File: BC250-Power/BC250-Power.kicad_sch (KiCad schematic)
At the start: 41 parts, among them J1 Conn_01x02_Pin, J2 Conn_01x02_Pin, J3 Conn_01x02_Pin, J4 Conn_01x03_Pin, J5 Conn_02x04_Odd_Even, J6 Conn_02x25_Row_Letter_First, J7 Conn_01x02_Pin, J8 Conn_01x02_Pin, M1 Fan_4pin, M2 Fan_4pin, M3 Fan_4pin, M4 Fan_4pin, Q1 BSS138, SW1 SW_Push, U1 NE555D, U2 TL082, U3 74LVC2G14, U4 L78L05_SO8

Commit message: Add values for fan circuit passives
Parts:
- added Q2: BSS138, Package_TO_SOT_SMD:SOT-23, symbol Transistor_FET:BSS138
- added R14: 10k, Resistor_SMD:R_0603_1608Metric, symbol Device:R
- C1, C2: value C -> 1uF
- R1, R2: value R -> 220
- R10, R13: value 10K -> 10k
- R11: value 1K -> 1k
- R12: value 100K -> 100k
- R3: value 100k -> 56k
- R6: value R -> 150
- R7: value R -> 2k
- R8, R9: value R -> 1k
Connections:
- net +5V: now also R14.1
- net GND: now also Q2.2 (S)
- net PWM_OUT: now also Q2.3 (D), R14.2; no longer R9.1, U2.7
- net at R3.2, R4.2, R5.1: now also U2.6 (-); no longer U2.5 (+)
- net at C3.1, R7.2, U1.2 (TR)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: now also U2.5 (+); no longer U2.6 (-)
- new net: Q2.1 (G), R9.1, U2.7
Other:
- note added: "Added the driver MOSFET to be sure to get down to the negative rail (cheap op-amps don't make it down under 0.7V or so). With assembly costs, it may make sense to use a rail-to-rail op-amp like the MCP6497. Note that the MOSFET is an inverter."
- note added: "Circuit from https://electronics.stackexchange.com/questions/186841"
- note added: "R/C values chosen from experimentation in Falstad simulator; could be improved (https://tinyurl.com/28phlmzg)"
- note added: "R7 = 0.481/(F*C) = 1923 (at 2000, F becomes 24kHz) R8 = R7 / 2 = 1000 R6 = 0.15 * R8 = 150"
- moved on the sheet: U2B

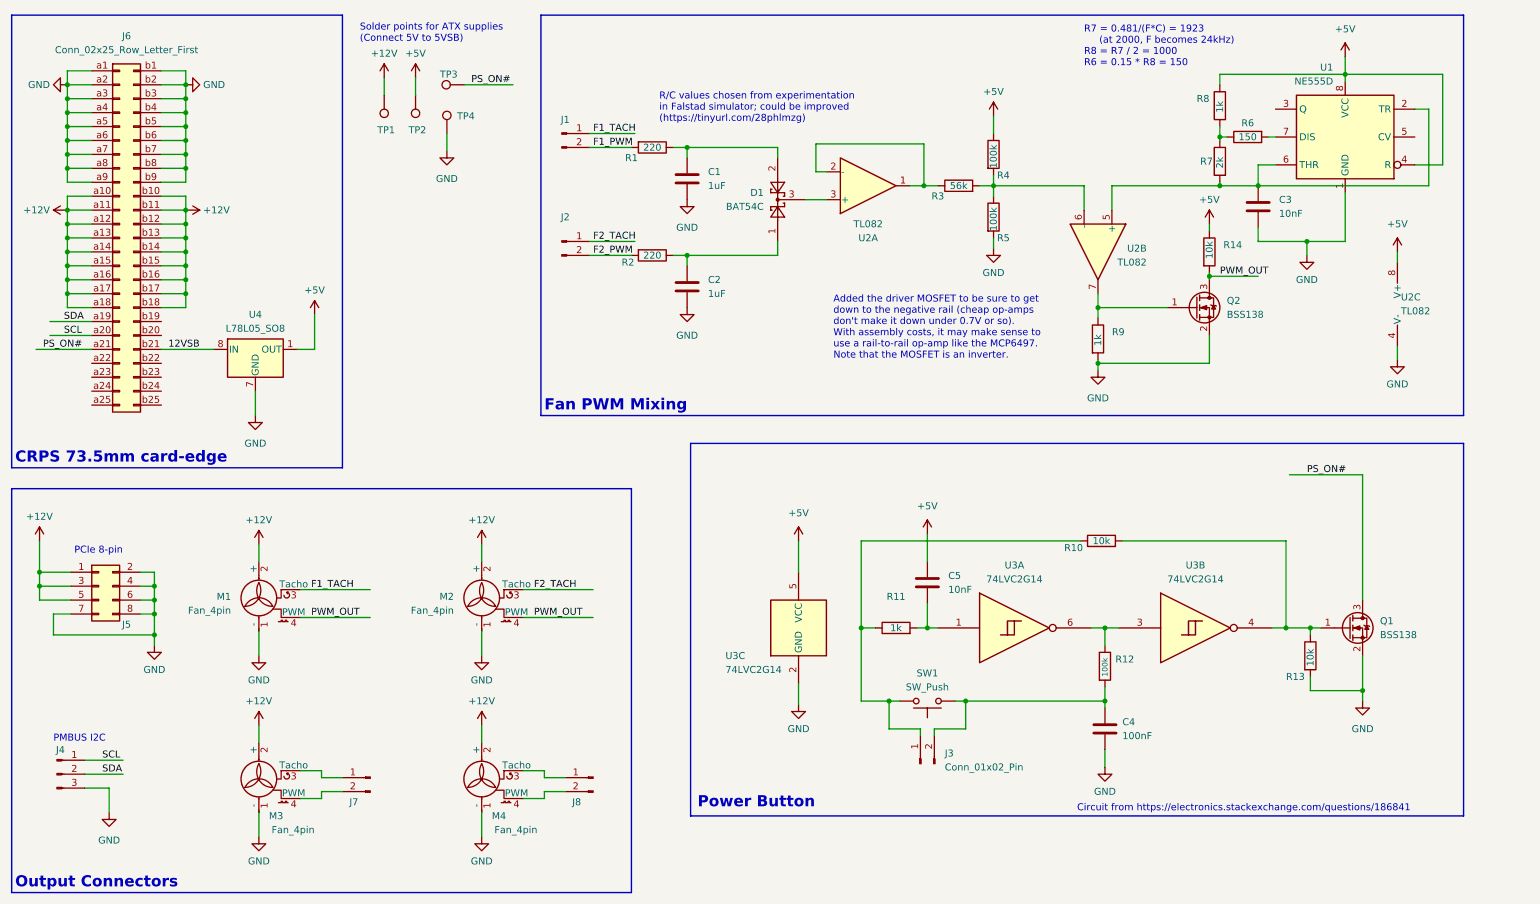
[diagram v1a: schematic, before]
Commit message: Add and associate S-50L-2.54-5 model
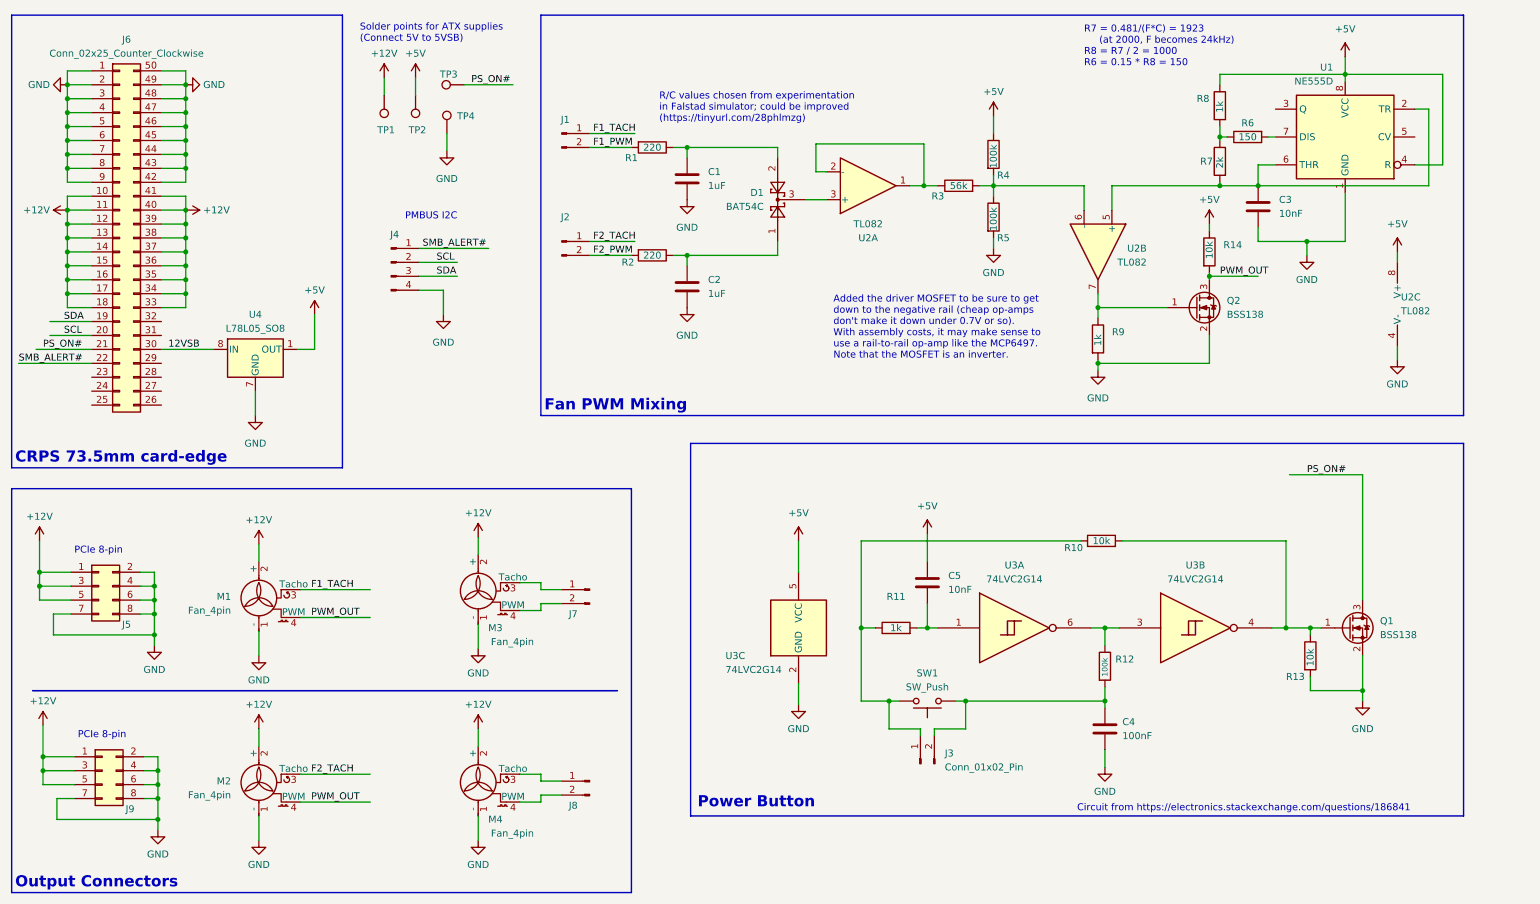
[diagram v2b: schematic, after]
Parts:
- removed J4: Conn_01x03_Pin, Connector_PinHeader_2.54mm:PinHeader_1x03_P2.54mm_Vertical, symbol Connector:Conn_01x03_Pin
- removed J6: Conn_02x25_Row_Letter_First, symbol Connector_Generic:Conn_02x25_Row_Letter_First
- added J4: Conn_01x04_Pin, Connector_PinHeader_2.54mm:PinHeader_1x04_P2.54mm_Vertical, symbol Connector:Conn_01x04_Pin
- added J6: Conn_02x25_Counter_Clockwise, BC250-Footprints:S-50L-2.54-5, symbol Connector_Generic:Conn_02x25_Counter_Clockwise
- added J9: Conn_02x04_Odd_Even, symbol Connector_Generic:Conn_02x04_Odd_Even
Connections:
- net +12V: now also J6.10 (Pin_10), J6.11 (Pin_11), J6.12 (Pin_12), J6.13 (Pin_13), J6.14 (Pin_14), J6.15 (Pin_15), J6.16 (Pin_16), J6.17 (Pin_17), J6.18 (Pin_18), J6.33 (Pin_33), J6.34 (Pin_34), J6.35 (Pin_35), J6.36 (Pin_36), J6.37 (Pin_37), J6.38 (Pin_38), J6.39 (Pin_39), J6.40 (Pin_40), J6.41 (Pin_41), J9.1 (Pin_1), J9.3 (Pin_3), J9.5 (Pin_5)
- net 12VSB: now also J6.30 (Pin_30)
- net GND: now also J4.4 (Pin_4), J6.1 (Pin_1), J6.2 (Pin_2), J6.3 (Pin_3), J6.4 (Pin_4), J6.42 (Pin_42), J6.43 (Pin_43), J6.44 (Pin_44), J6.45 (Pin_45), J6.46 (Pin_46), J6.47 (Pin_47), J6.48 (Pin_48), J6.49 (Pin_49), J6.5 (Pin_5), J6.50 (Pin_50), J6.6 (Pin_6), J6.7 (Pin_7), J6.8 (Pin_8), J6.9 (Pin_9), J9.2 (Pin_2), J9.4 (Pin_4), J9.6 (Pin_6), J9.7 (Pin_7), J9.8 (Pin_8)
- net PS_ON#: now also J6.21 (Pin_21)
- net SCL: now also J4.2 (Pin_2), J6.20 (Pin_20)
- net SDA: now also J4.3 (Pin_3), J6.19 (Pin_19)
- new net SMB_ALERT#: J4.1 (Pin_1), J6.22 (Pin_22)
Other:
- moved on the sheet: J7, J8, M2, M3, M4

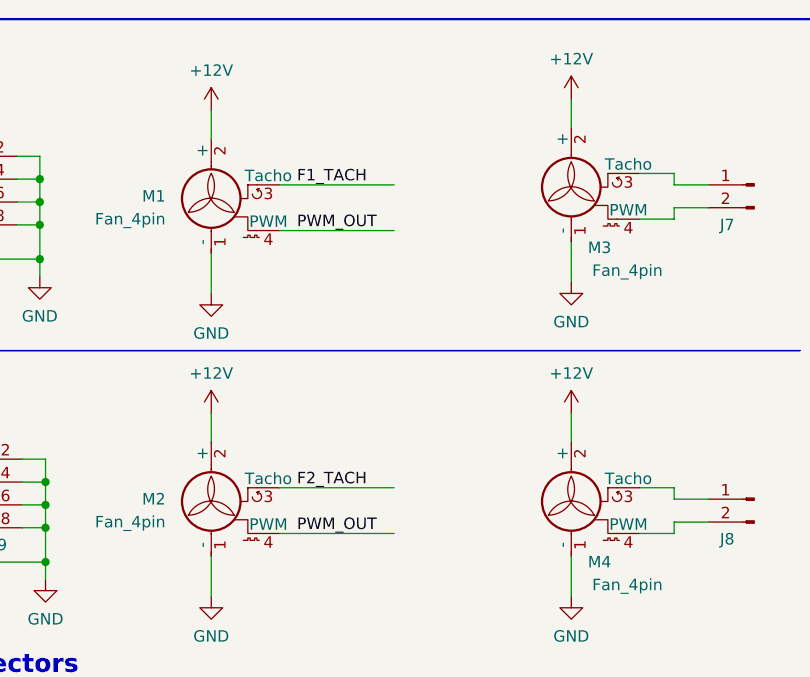
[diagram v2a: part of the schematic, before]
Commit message: Update to KiCad 9 and redo holes in card-edge footprint
Kicad 7 doesn't render shells in STEPs correctly
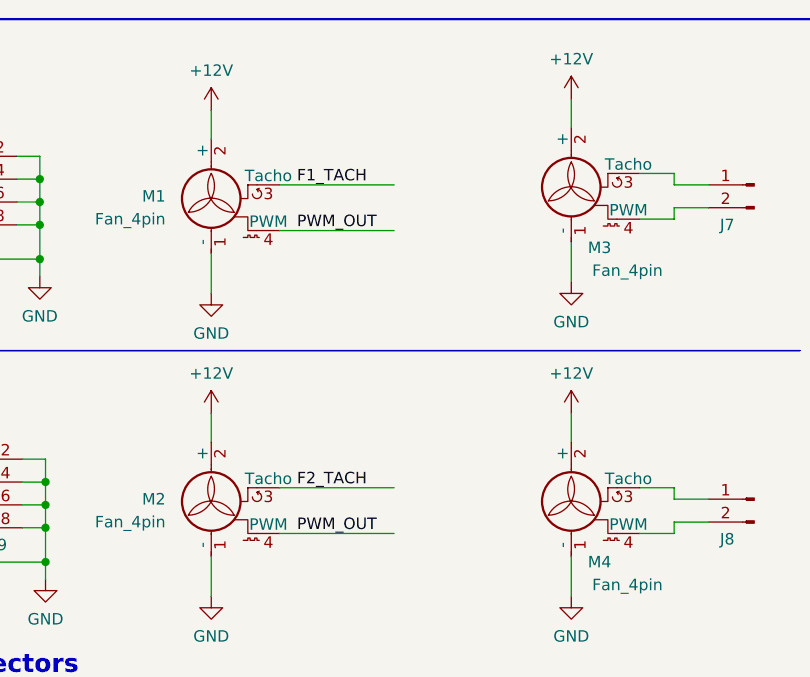
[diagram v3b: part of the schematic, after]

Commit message: Start layout and fix pinning
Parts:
- removed Q1: BSS138, Package_TO_SOT_SMD:SOT-23, symbol Transistor_FET:BSS138
- removed R13: 10k, Resistor_SMD:R_0603_1608Metric, symbol Device:R
- J5, J9: footprint (none) -> BC250-Footprints:GPU-8P-PCB; symbol Connector_Generic:Conn_02x04_Odd_Even -> Connector_Generic:Conn_02x04_Top_Bottom
- SW1: footprint (none) -> Button_Switch_SMD:SW_SPST_TL3305A
- TP1, TP2, TP3, TP4: footprint (none) -> TestPoint:TestPoint_Loop_D2.60mm_Drill1.6mm_Beaded
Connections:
- net +12V: now also J5.2 (Pin_2), J6.42 (Pin_42), J6.43 (Pin_43), J6.8 (Pin_8), J6.9 (Pin_9), J9.2 (Pin_2); no longer J5.5 (Pin_5), J6.17 (Pin_17), J6.18 (Pin_18), J6.33 (Pin_33), J6.34 (Pin_34), J9.5 (Pin_5)
- net 12VSB: now also J6.46 (Pin_46); no longer J6.30 (Pin_30)
- net GND: now also J5.5 (Pin_5), J6.17 (Pin_17), J6.18 (Pin_18), J6.19 (Pin_19), J6.20 (Pin_20), J6.21 (Pin_21), J6.22 (Pin_22), J6.23 (Pin_23), J6.24 (Pin_24), J6.25 (Pin_25), J6.26 (Pin_26), J6.27 (Pin_27), J6.28 (Pin_28), J6.29 (Pin_29), J6.30 (Pin_30), J6.31 (Pin_31), J6.32 (Pin_32), J6.33 (Pin_33), J6.34 (Pin_34), J9.5 (Pin_5); no longer J5.2 (Pin_2), J6.1 (Pin_1), J6.2 (Pin_2), J6.3 (Pin_3), J6.4 (Pin_4), J6.42 (Pin_42), J6.43 (Pin_43), J6.44 (Pin_44), J6.45 (Pin_45), J6.46 (Pin_46), J6.47 (Pin_47), J6.48 (Pin_48), J6.49 (Pin_49), J6.5 (Pin_5), J6.50 (Pin_50), J6.6 (Pin_6), J6.7 (Pin_7), J6.8 (Pin_8), J6.9 (Pin_9), J9.2 (Pin_2)
- net PS_ON#: now also J6.5 (Pin_5), R10.2, U3.4; no longer J6.21 (Pin_21)
- net SCL: now also J6.6 (Pin_6); no longer J6.20 (Pin_20)
- net SDA: now also J6.7 (Pin_7); no longer J6.19 (Pin_19)
- net SMB_ALERT#: now also J6.4 (Pin_4); no longer J6.22 (Pin_22)
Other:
- moved on the sheet: C1, C2, C3, C4, C5, D1, J1, J2, J3, J4, J5, J6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

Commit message: First pass at routing
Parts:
- removed J7, J8: Conn_01x02_Pin, Connector_PinHeader_2.54mm:PinHeader_1x02_P2.54mm_Horizontal, symbol Connector:Conn_01x02_Pin
- removed M3, M4: Fan_4pin, Connector:FanPinHeader_1x04_P2.54mm_Vertical, symbol Motor:Fan_4pin
- J4: footprint Connector_PinHeader_2.54mm:PinHeader_1x04_P2.54mm_Vertical -> Connector_PinHeader_2.54mm:PinHeader_1x04_P2.54mm_Horizontal
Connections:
- net F1_PWM: now also J1.1 (Pin_1); no longer J1.2 (Pin_2)
- net F1_TACH: now also J1.2 (Pin_2); no longer J1.1 (Pin_1)
- net GND: now also J4.1 (Pin_1); no longer J4.4 (Pin_4)
- net SCL: now also J4.3 (Pin_3); no longer J4.2 (Pin_2)
- net SDA: now also J4.2 (Pin_2); no longer J4.3 (Pin_3)
- net SMB_ALERT#: now also J4.4 (Pin_4); no longer J4.1 (Pin_1)
- net at C2.1, R2.1: now also D1.2; no longer D1.1
- net at C1.1, R1.1: now also D1.1; no longer D1.2
- net at C4.1, R12.2: now also J3.1 (Pin_1), SW1.2; no longer J3.2 (Pin_2), SW1.1
- net at R10.1, R11.1: now also J3.2 (Pin_2), SW1.1; no longer J3.1 (Pin_1), SW1.2
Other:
- moved on the sheet: C4, C5, J3, J4, R10, R11, R12, SW1, TP1, TP2, TP3, TP4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

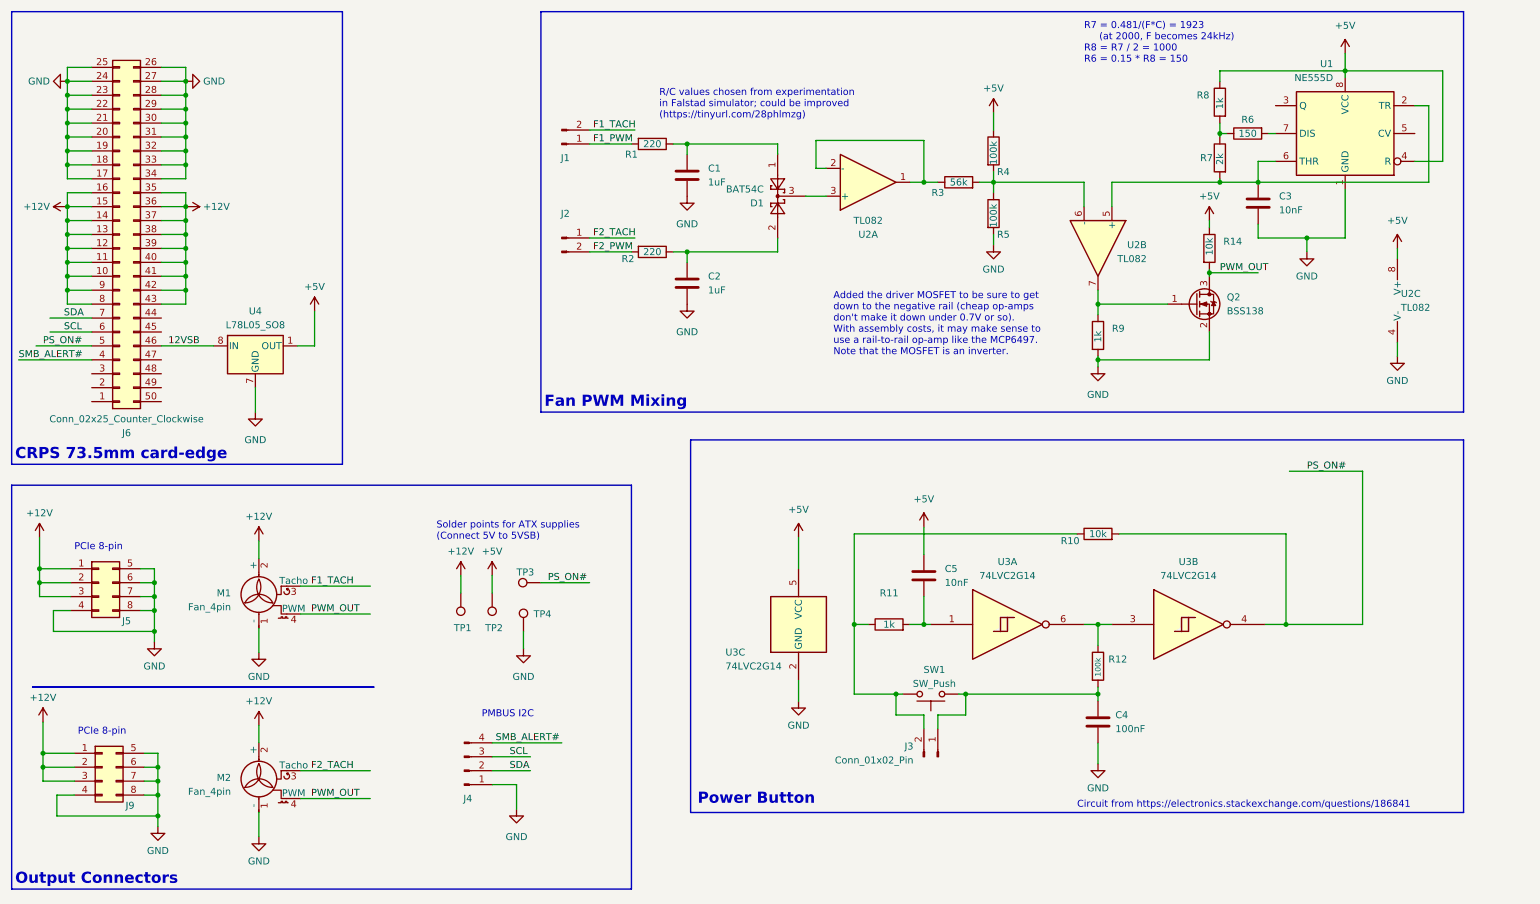
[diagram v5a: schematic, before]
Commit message: Add V0.2 of dual BC-250 CRPS breakout
- Organize fab layer
- Un-mirror edge connector (was reversing 12VSB and PS_ON# - oops)
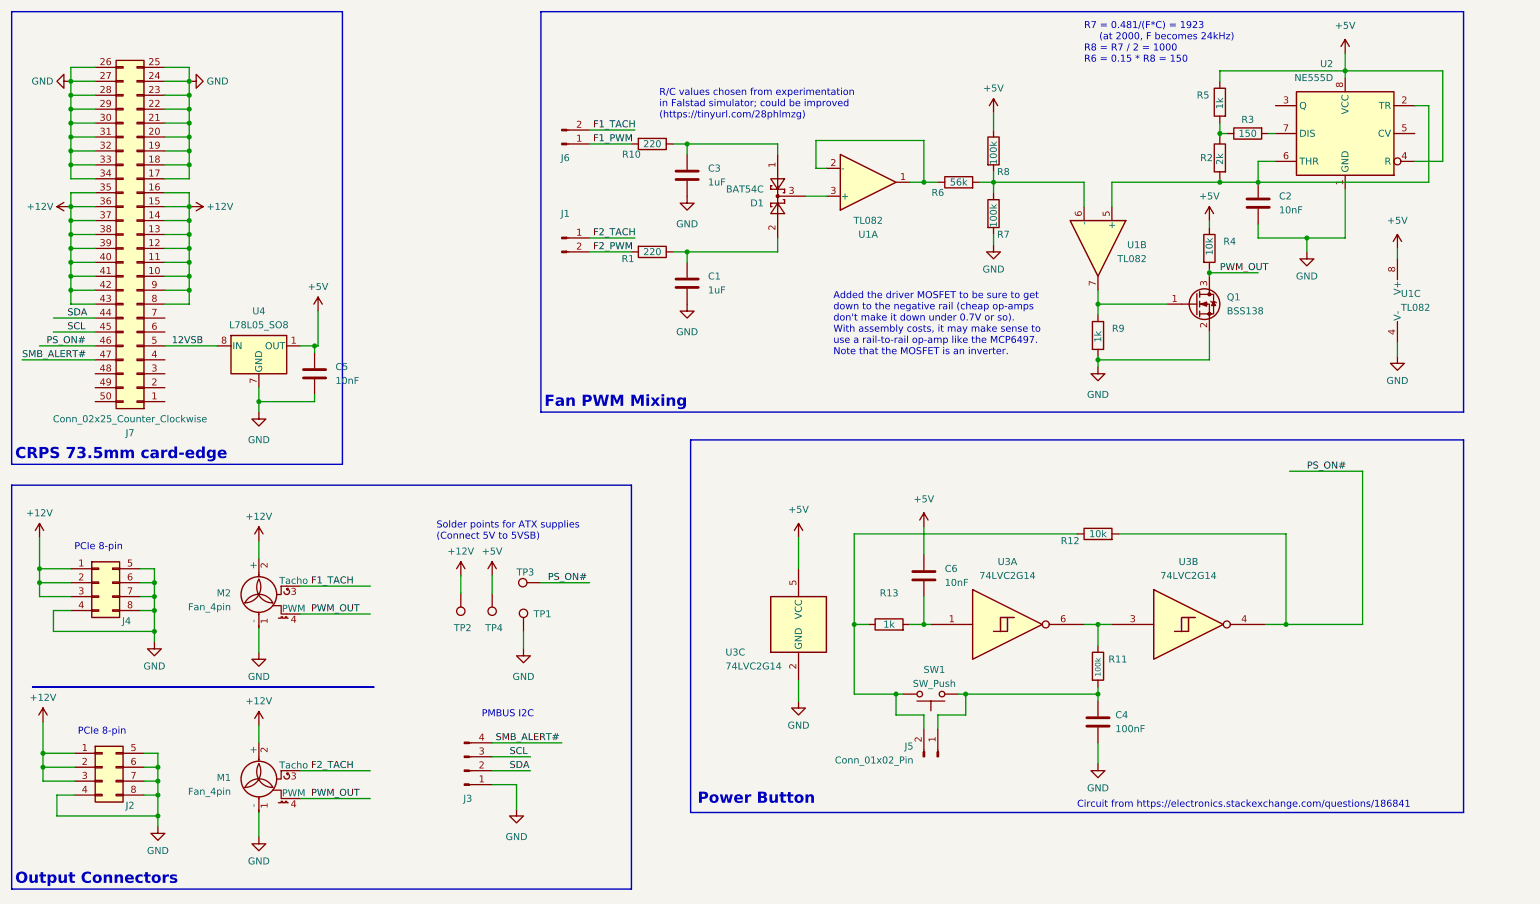
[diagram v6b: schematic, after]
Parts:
- added C5: 10nF, Capacitor_SMD:C_0603_1608Metric, symbol Device:C
- renumbered C2 to C1, C3 to C2, C1 to C3, C5 to C6, J2 to J1, J9 to J2, J4 to J3, J5 to J4, J3 to J5, J1 to J6, J6 to J7, M2 to M1, M1 to M2, Q2 to Q1, R2 to R1, R1 to R10, R12 to R11, R10 to R12, R11 to R13, R7 to R2, R6 to R3, R14 to R4, R8 to R5, R3 to R6, R5 to R7, R4 to R8, TP4 to TP1, TP1 to TP2, TP2 to TP4, U2 to U1, U1 to U2
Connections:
- net +5V: now also C5.1
- net 12VSB: now also J7.5 (Pin_5); no longer J7.46 (Pin_46)
- net GND: now also C5.2
- net PS_ON#: now also J7.46 (Pin_46); no longer J7.5 (Pin_5)
- net SCL: now also J7.45 (Pin_45); no longer J7.6 (Pin_6)
- net SDA: now also J7.44 (Pin_44); no longer J7.7 (Pin_7)
- net SMB_ALERT#: now also J7.47 (Pin_47); no longer J7.4 (Pin_4)
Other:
- moved on the sheet: J7, U4
